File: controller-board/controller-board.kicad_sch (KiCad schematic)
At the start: 169 parts, among them J1 Conn_01x02, J2 Conn_01x02, J3 Conn_01x02, J4 Conn_01x02, J5 Conn_01x03, J6 Conn_01x02, Q1 SQS460EN, Q2 DGD0216, SW1 EG1271, U1 CAT4201, U10 CAT4201, U11 CAT4201, U12 CAT4201, U13 CAT4201, U14 CAT4201, U15 CAT4201, U17 CAT4201, U18 CAT4201, U2 PocketBeagle, U3 LTC3624, U4 CAT4201, U5 CAT4201, U6 CAT4201, U7 MCP4728, U8 ADS1015IRUGR, U9 ADS1015IRUGR

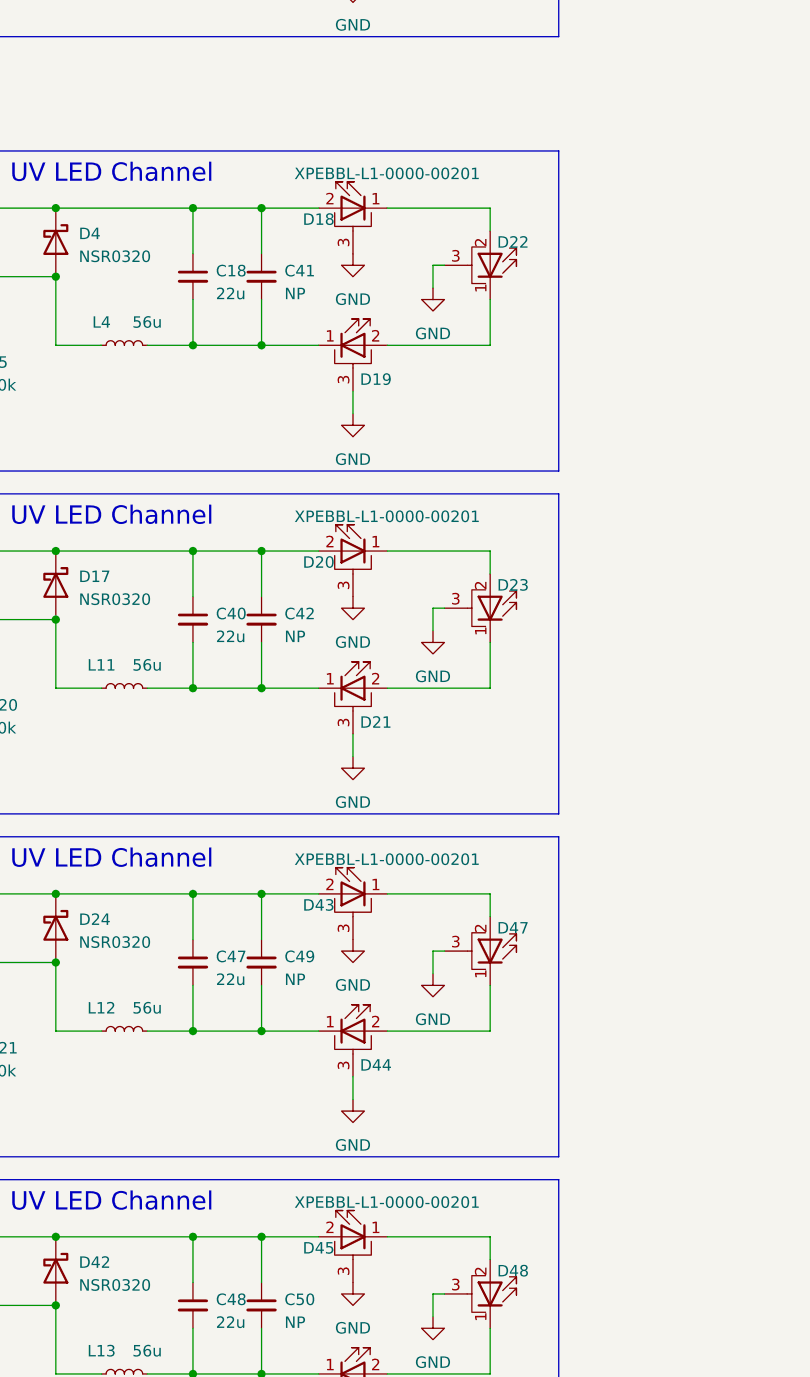
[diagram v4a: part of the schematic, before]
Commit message: Added thermal vias for LEDS and soldermask openings to bypass the LEDs
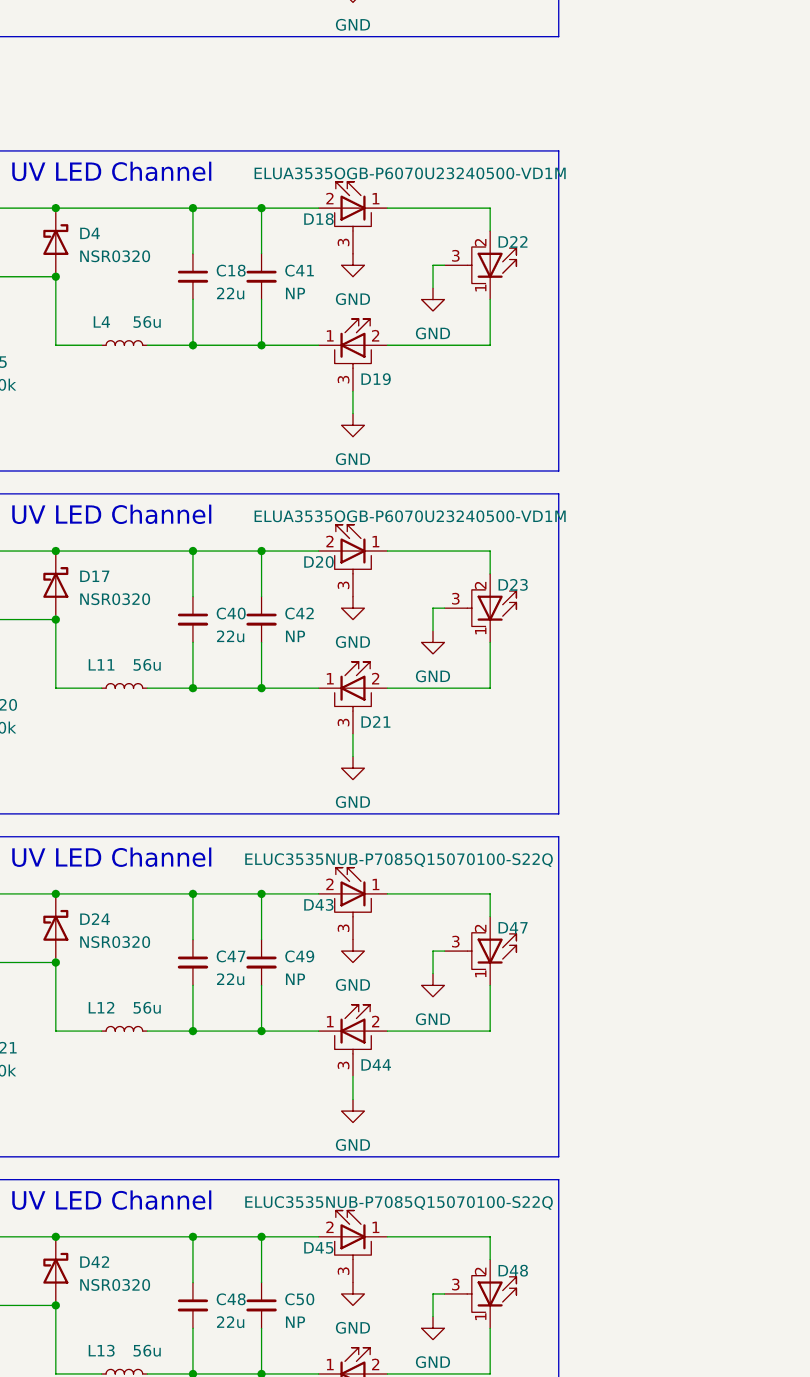
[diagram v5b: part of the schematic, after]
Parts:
- D18, D19, D20, D21, D22, D23: value XPEBBL-L1-0000-00201 -> ELUA3535OGB-P6070U23240500-VD1M
- D43, D44, D45, D46, D47, D48: value XPEBBL-L1-0000-00201 -> ELUC3535NUB-P7085Q15070100-S22Q
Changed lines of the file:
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@@
       (effects (font (size 1.27 1.27)))
     )
-    (property "Value" "XPEBBL-L1-0000-00201" (at 280.67 351.79 0)
+    (property "Value" "ELUC3535NUB-P7085Q15070100-S22Q" (at 281.94 351.79 0)
       (effects (font (size 1.27 1.27)))
     )
@@
       (effects (font (size 1.27 1.27)))
     )
-    (property "Value" "XPEBBL-L1-0000-00201" (at 295.91 369.57 0)
+    (property "Value" "ELUC3535NUB-P7085Q15070100-S22Q" (at 295.91 369.57 0)
       (effects (font (size 1.27 1.27)) (justify left) hide)
     )
@@
       (effects (font (size 1.27 1.27)))
     )
-    (property "Value" "XPEBBL-L1-0000-00201" (at 276.86 290.83 0)
+    (property "Value" "ELUA3535OGB-P6070U23240500-VD1M" (at 276.86 290.83 0)
       (effects (font (size 1.27 1.27)) hide)
     )
@@
       (effects (font (size 1.27 1.27)))
     )
-    (property "Value" "XPEBBL-L1-0000-00201" (at 276.86 405.13 0)
+    (property "Value" "ELUC3535NUB-P7085Q15070100-S22Q" (at 276.86 405.13 0)
       (effects (font (size 1.27 1.27)) hide)
     )
@@
       (effects (font (size 1.27 1.27)))
     )
-    (property "Value" "XPEBBL-L1-0000-00201" (at 295.91 293.37 0)
+    (property "Value" "ELUA3535OGB-P6070U23240500-VD1M" (at 295.91 293.37 0)
       (effects (font (size 1.27 1.27)) (justify left) hide)
     )
@@
       (effects (font (size 1.27 1.27)))
     )
-    (property "Value" "XPEBBL-L1-0000-00201" (at 295.91 331.47 0)
+    (property "Value" "ELUA3535OGB-P6070U23240500-VD1M" (at 295.91 331.47 0)
       (effects (font (size 1.27 1.27)) (justify left) hide)
     )
@@
       (effects (font (size 1.27 1.27)))
     )
-    (property "Value" "XPEBBL-L1-0000-00201" (at 295.91 407.67 0)
+    (property "Value" "ELUC3535NUB-P7085Q15070100-S22Q" (at 295.91 407.67 0)
       (effects (font (size 1.27 1.27)) (justify left) hide)
     )
@@
       (effects (font (size 1.27 1.27)))
     )
-    (property "Value" "XPEBBL-L1-0000-00201" (at 280.67 313.69 0)
+    (property "Value" "ELUA3535OGB-P6070U23240500-VD1M" (at 283.21 313.69 0)
       (effects (font (size 1.27 1.27)))
     )
@@
       (effects (font (size 1.27 1.27)))
     )
-    (property "Value" "XPEBBL-L1-0000-00201" (at 276.86 328.93 0)
+    (property "Value" "ELUA3535OGB-P6070U23240500-VD1M" (at 276.86 328.93 0)
       (effects (font (size 1.27 1.27)) hide)
     )
@@
       (effects (font (size 1.27 1.27)))
     )
-    (property "Value" "XPEBBL-L1-0000-00201" (at 276.86 367.03 0)
+    (property "Value" "ELUC3535NUB-P7085Q15070100-S22Q" (at 276.86 367.03 0)
       (effects (font (size 1.27 1.27)) hide)
     )
@@
       (effects (font (size 1.27 1.27)))
     )
-    (property "Value" "XPEBBL-L1-0000-00201" (at 280.67 389.89 0)
+    (property "Value" "ELUC3535NUB-P7085Q15070100-S22Q" (at 281.94 389.89 0)
       (effects (font (size 1.27 1.27)))
     )
@@
       (effects (font (size 1.27 1.27)))
     )
-    (property "Value" "XPEBBL-L1-0000-00201" (at 280.67 275.59 0)
+    (property "Value" "ELUA3535OGB-P6070U23240500-VD1M" (at 283.21 275.59 0)
       (effects (font (size 1.27 1.27)))
     )
